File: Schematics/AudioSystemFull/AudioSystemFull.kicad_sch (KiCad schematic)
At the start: 285 parts, among them IC1 TDA1558Q, J1 SJ1-3515-SMT-TR-BE, J3 Conn_Display_Buttons, J6 Conn_ISO, U1 LP3856ES-5.0, U10 LT3015EQ-5PBF, U11 OPA2134, U12 OPA2134, U13 OPA2134, U14 OPA2134, U15 OPA2134, U16 OPA2134, U17 OPA2134, U18 OPA2134, U19 OPA2134, U2 DEVKIT_V1_ESP32-WROOM-32, U20 OPA2134, U21 OPA2134, U22 OPA2134, U23 OPA2134, U24 OPA2134, U25 OPA2134, U26 OPA2134, U27 OPA2134, U28 OPA2134, U3 PCM5102A, U4 OPA2134, U5 LP5907MFX-3.3, U6 LMR51420XFDDCR, U7 LMR51420YFDDCR, U8 LP5907MFX-3.3, U9 LMR51430YFDDCR

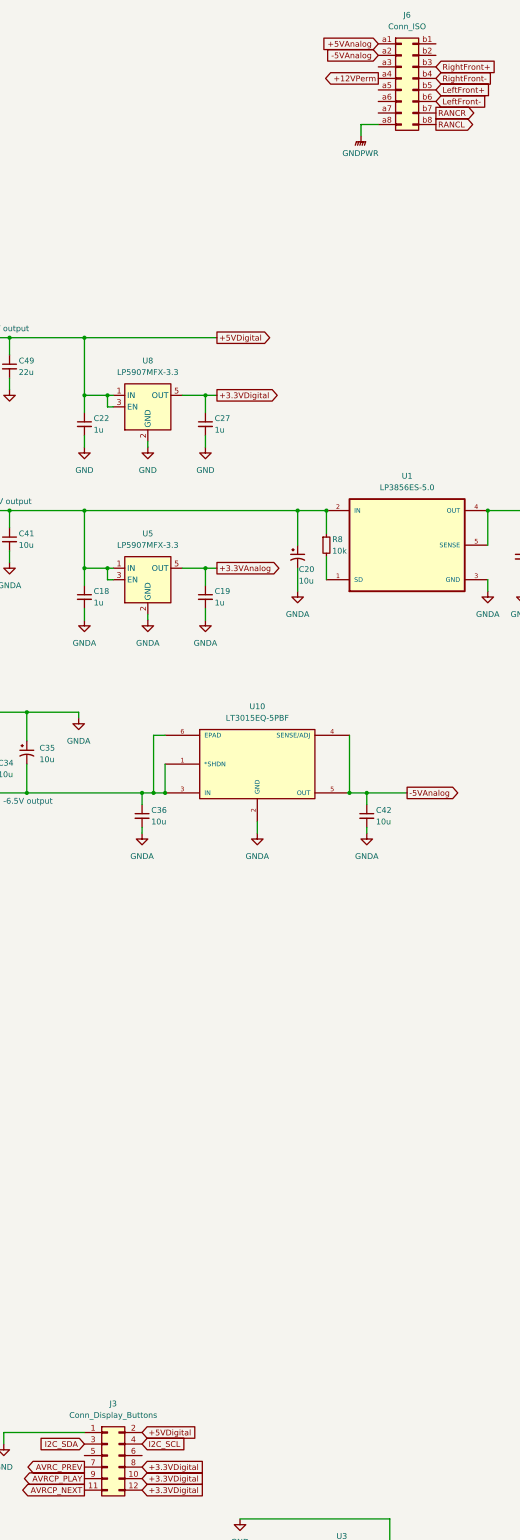
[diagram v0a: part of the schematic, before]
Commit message: organize footprints by purpose
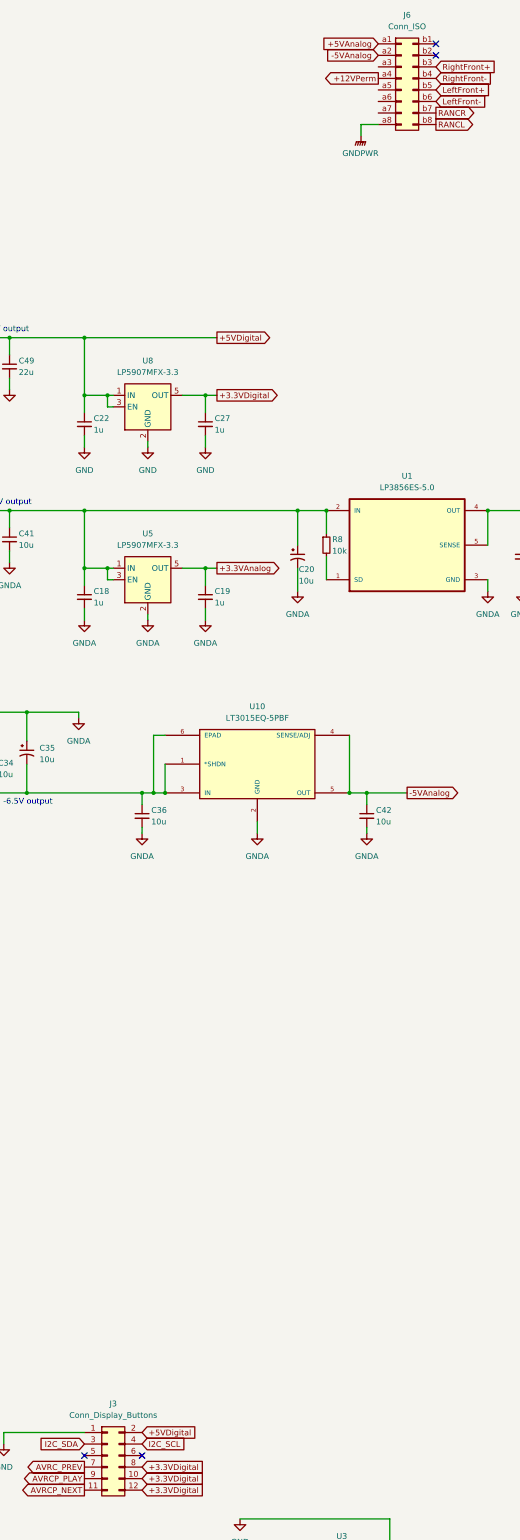
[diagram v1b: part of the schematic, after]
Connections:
- no-connect marks 30 -> 34
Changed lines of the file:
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@@
+	)
+	(no_connect
+		(at 273.05 35.56)
 	)
 	(no_connect
@@
 	)
 	(no_connect
+		(at 208.28 346.71)
+	)
+	(no_connect
 		(at 125.73 397.51)
 	)
@@
 	)
 	(no_connect
+		(at 273.05 38.1)
+	)
+	(no_connect
 		(at 166.37 369.57)
 	)
@@
 	)
 	(no_connect
+		(at 195.58 346.71)
+	)
+	(no_connect

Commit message: footprint placement part 1
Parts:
- C11, C12, C3, C4: footprint AudioSystemFootprintLibrary:UCZ1J100MCL1GS -> Capacitor_SMD:C_1206_3216Metric_Pad1.33x1.80mm_HandSolder; MANUFACTURER_PART_NUMBER UCZ1J100MCL1GS -> 293D106X96R3A2TE3
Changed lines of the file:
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@@
 			)
 		)
-		(property "Footprint" "AudioSystemFootprintLibrary:UCZ1J100MCL1GS"
+		(property "Footprint" "Capacitor_SMD:C_1206_3216Metric_Pad1.33x1.80mm_HandSolder"
 			(at 218.44 405.13 0)
 			(effects
@@
 			)
 		)
-		(property "MANUFACTURER_PART_NUMBER" "UCZ1J100MCL1GS"
+		(property "MANUFACTURER_PART_NUMBER" "293D106X96R3A2TE3"
 			(at 218.44 405.13 0)
 			(effects
@@
 			)
 		)
-		(property "Footprint" "AudioSystemFootprintLibrary:UCZ1J100MCL1GS"
+		(property "Footprint" "Capacitor_SMD:C_1206_3216Metric_Pad1.33x1.80mm_HandSolder"
 			(at 279.4 401.32 0)
 			(effects
@@
 			)
 		)
-		(property "MANUFACTURER_PART_NUMBER" "UCZ1J100MCL1GS"
+		(property "MANUFACTURER_PART_NUMBER" "293D106X96R3A2TE3"
 			(at 279.4 401.32 0)
 			(effects
@@
 			)
 		)
-		(property "Footprint" "AudioSystemFootprintLibrary:UCZ1J100MCL1GS"
+		(property "Footprint" "Capacitor_SMD:C_1206_3216Metric_Pad1.33x1.80mm_HandSolder"
 			(at 218.44 394.97 0)
 			(effects
@@
 			)
 		)
-		(property "MANUFACTURER_PART_NUMBER" "UCZ1J100MCL1GS"
+		(property "MANUFACTURER_PART_NUMBER" "293D106X96R3A2TE3"
 			(at 218.44 394.97 0)
 			(effects
@@
 			)
 		)
-		(property "Footprint" "AudioSystemFootprintLibrary:UCZ1J100MCL1GS"
+		(property "Footprint" "Capacitor_SMD:C_1206_3216Metric_Pad1.33x1.80mm_HandSolder"
 			(at 279.4 373.38 0)
 			(effects
@@
 			)
 		)
-		(property "MANUFACTURER_PART_NUMBER" "UCZ1J100MCL1GS"
+		(property "MANUFACTURER_PART_NUMBER" "293D106X96R3A2TE3"
 			(at 279.4 373.38 0)
 			(effects

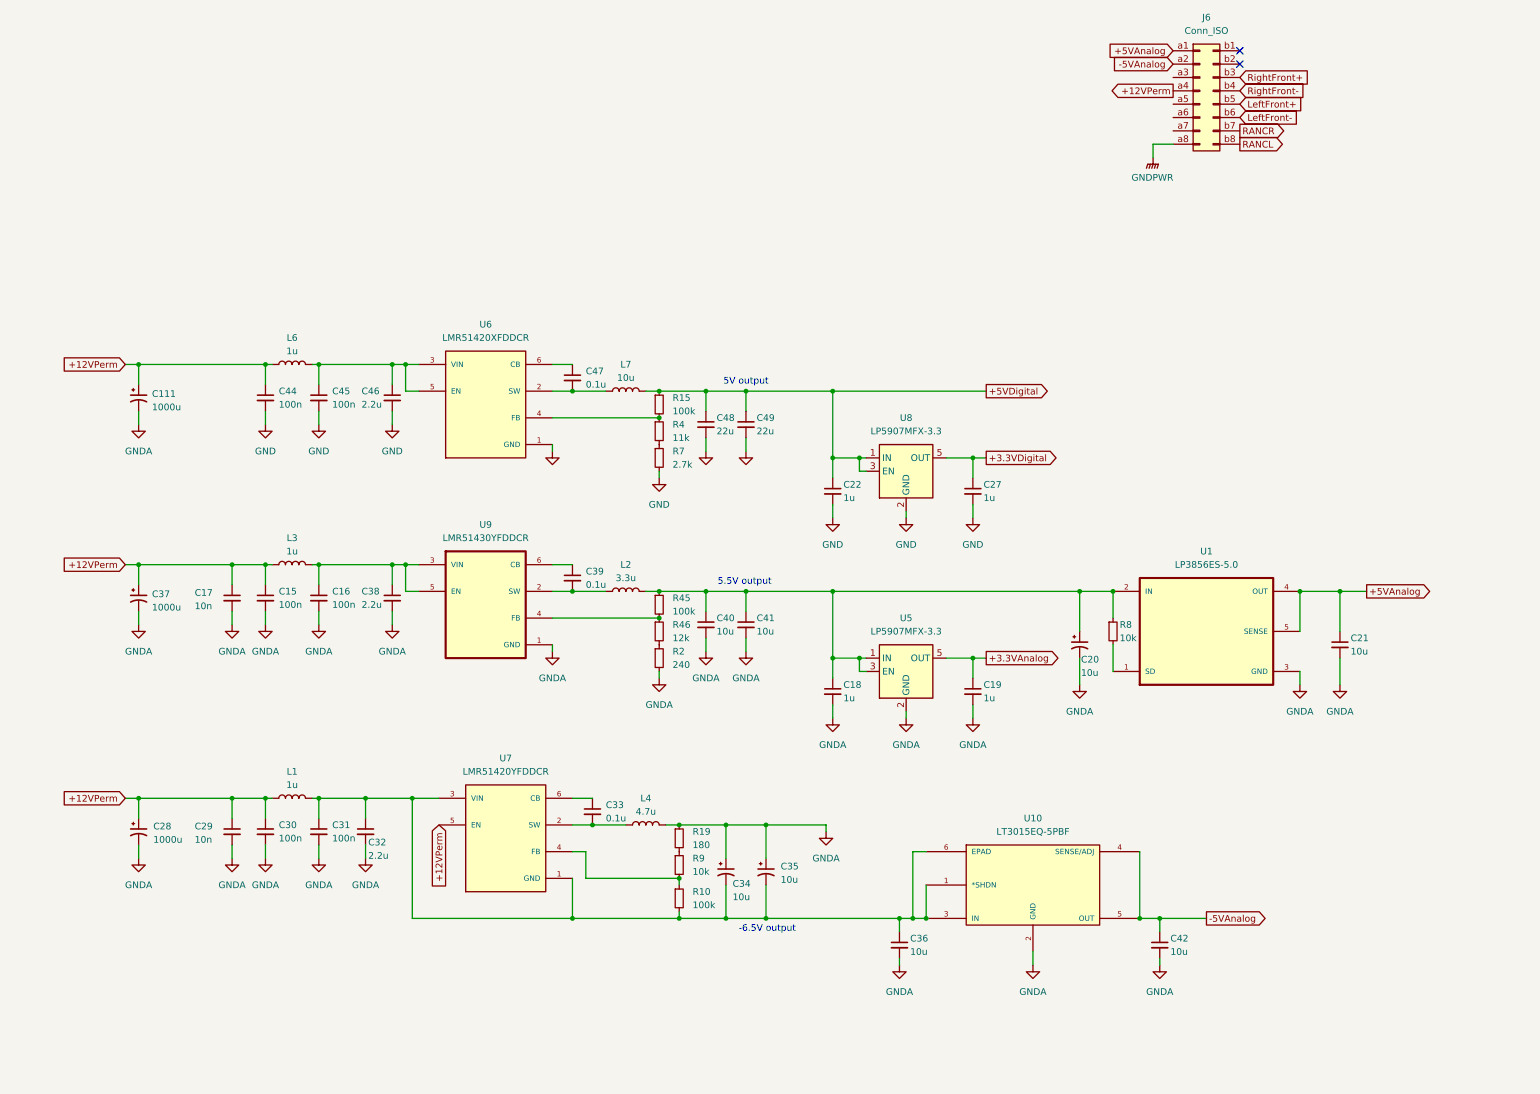
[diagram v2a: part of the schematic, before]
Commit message: footprint placement possibly done, minor schematic changes
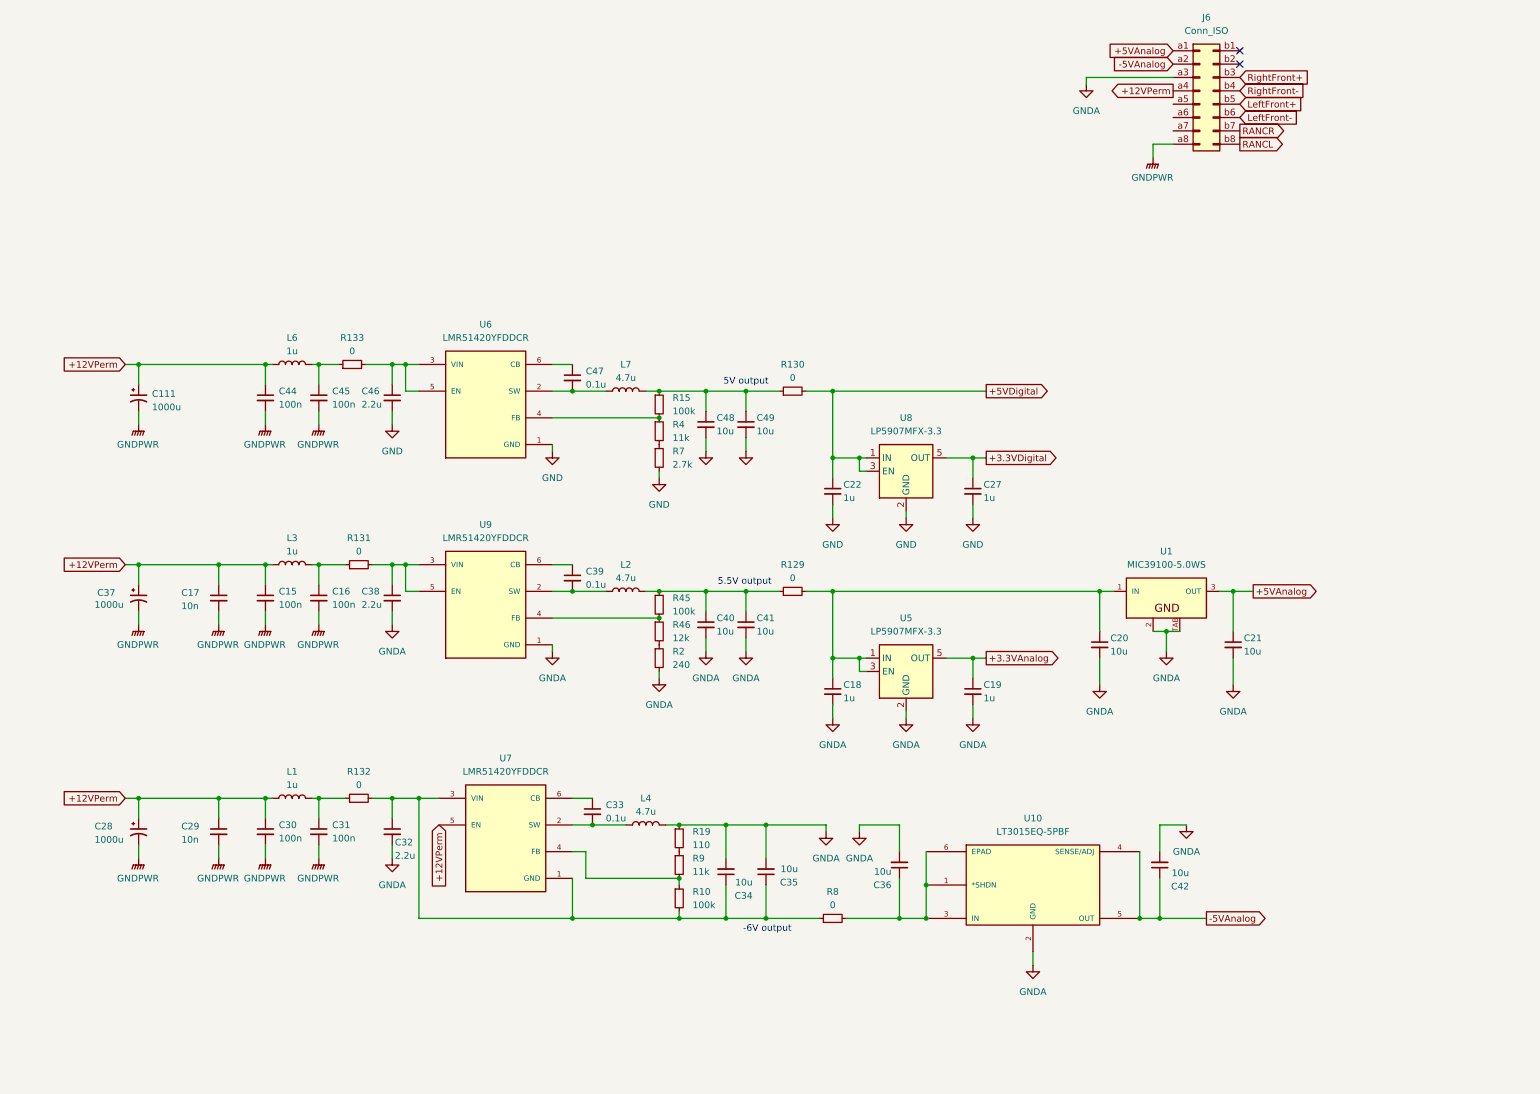
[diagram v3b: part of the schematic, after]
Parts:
- removed C20, C34, C35: 10u, AudioSystemFootprintLibrary:UCZ1J100MCL1GS, symbol Device:C_Polarized_Small_US
- removed U1: LP3856ES-5.0, AudioSystemFootprintLibrary:LP3856ES-5.0, symbol AudioSystemSymbolLibrary:LP3856ES-5.0
- removed U6: LMR51420XFDDCR, AudioSystemFootprintLibrary:LMR51420XFDDCR, symbol AudioSystemSymbolLibrary:LMR51420XFDDCR
- removed U9: LMR51430YFDDCR, AudioSystemFootprintLibrary:LMR51430YFDDCR, symbol AudioSystemSymbolLibrary:LMR51430YFDDCR
- added C20, C34, C35: 10u, Capacitor_SMD:C_0805_2012Metric_Pad1.18x1.45mm_HandSolder, symbol Device:C_Small
- added R129, R130, R131, R132, R133: 0, Resistor_SMD:R_0805_2012Metric_Pad1.20x1.40mm_HandSolder, symbol Device:R_Small
- added U1: MIC39100-5.0WS, AudioSystemFootprintLibrary:MIC39100-5.0WS, symbol AudioSystemSymbolLibrary:MIC39100-5.0WS
- added U6, U9: LMR51420YFDDCR, AudioSystemFootprintLibrary:LMR51420YFDDCR, symbol AudioSystemSymbolLibrary:LMR51420YFDDCR
- C1, C10, C100, C101, C102, C103, C104, C105, C106, C107, C108, C109, C110, C13, C14, C15, C16, C17, C18, C19, C2, C21, C22, C23, C24, C25, C27, C29, C30, C31, C32, C33, C36, C38, C39, C40, C41, C42, C43, C44, C45, C46, C47, C5, C50, C51, C52, C53, C54, C55, C56, C57, C58, C59, C6, C60, C61, C62, C63, C64, C65, C66, C67, C68, C69, C7, C70, C71, C72, C73, C74, C75, C76, C77, C78, C79, C8, C80, C81, C82, C83, C84, C85, C86, C87, C88, C89, C9, C90, C91, C92, C93, C94, C95, C96, C97, C98, C99: footprint Capacitor_SMD:C_1206_3216Metric_Pad1.33x1.80mm_HandSolder -> Capacitor_SMD:C_0805_2012Metric_Pad1.18x1.45mm_HandSolder
- C48, C49: value 22u -> 10u; footprint Capacitor_SMD:C_1210_3225Metric_Pad1.33x2.70mm_HandSolder -> Capacitor_SMD:C_0805_2012Metric_Pad1.18x1.45mm_HandSolder; MANUFACTURER_PART_NUMBER CL32B226KAJNNNE -> (none)
- L2: value 3.3u -> 4.7u; footprint AudioSystemFootprintLibrary:SRP5030T-3R3M -> AudioSystemFootprintLibrary:VLS6045EX-4R7M-H; MANUFACTURER_PART_NUMBER SRP5030T-3R3M -> (none)
- L7: value 10u -> 4.7u; footprint AudioSystemFootprintLibrary:SRR1280A-100M -> AudioSystemFootprintLibrary:VLS6045EX-4R7M-H; MANUFACTURER_PART_NUMBER SRR1280A-100M -> (none)
- R1, R10, R100, R101, R102, R103, R104, R105, R106, R107, R108, R109, R11, R110, R111, R112, R113, R114, R115, R116, R117, R118, R119, R12, R120, R121, R122, R123, R124, R125, R126, R127, R128, R13, R14, R15, R16, R17, R18, R2, R20, R21, R23, R25, R26, R27, R28, R29, R3, R30, R31, R33, R35, R36, R37, R38, R39, R4, R40, R41, R42, R43, R44, R45, R46, R47, R48, R49, R5, R50, R51, R53, R55, R56, R57, R58, R59, R6, R60, R61, R62, R63, R64, R65, R66, R67, R68, R69, R7, R70, R73, R74, R75, R76, R77, R78, R79, R80, R83, R84, R85, R86, R87, R88, R89, R90, R91, R92, R93, R94, R95, R96, R99: footprint Resistor_SMD:R_1206_3216Metric_Pad1.30x1.75mm_HandSolder -> Resistor_SMD:R_0805_2012Metric_Pad1.20x1.40mm_HandSolder
- R19: value 180 -> 110; footprint Resistor_SMD:R_1206_3216Metric_Pad1.30x1.75mm_HandSolder -> Resistor_SMD:R_0805_2012Metric_Pad1.20x1.40mm_HandSolder
- R8: value 10k -> 0; footprint Resistor_SMD:R_1206_3216Metric_Pad1.30x1.75mm_HandSolder -> Resistor_SMD:R_0805_2012Metric_Pad1.20x1.40mm_HandSolder; MANUFACTURER_PART_NUMBER RNCU1206BTE10K0 -> HRG3216P-1800-D-T1
- R9: value 10k -> 11k; footprint Resistor_SMD:R_1206_3216Metric_Pad1.30x1.75mm_HandSolder -> Resistor_SMD:R_0805_2012Metric_Pad1.20x1.40mm_HandSolder
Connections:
- net +5VAnalog: now also U1.3 (OUT)
- net +5VDigital: now also R130.2; no longer C48.1, C49.1, L7.2, R15.1
- net GND: now also U6.1 (GND); no longer C44.2, C45.2
- net GNDA: now also J6.a3 (Pin_a3), C20.2, C34.2, C35.2, U1.2, U1.TAB, U9.1 (GND); no longer C111.2, C15.2, C16.2, C17.2, C28.2, C29.2, C30.2, C31.2, C37.2
- net GNDPWR: now also C111.2, C15.2, C16.2, C17.2, C28.2, C29.2, C30.2, C31.2, C37.2, C44.2, C45.2
- net at C45.1, L6.2: now also R133.1; no longer C46.1
- net at C40.1, C41.1, L2.2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: now also R129.1; no longer C18.1, R8.1, U5.1 (IN), U5.3 (EN)
- net at C47.2, L7.1: now also U6.2 (SW)
- net at R15.2, R4.1: now also U6.4 (FB)
- net at C47.1: now also U6.6 (CB)
- net at C16.1, L3.2: now also R131.1; no longer C38.1
- net at C39.2, L2.1: now also U9.2 (SW)
- net at R8.2: now also C36.1, U10.1 (*SHDN), U10.3 (IN), U10.6 (EPAD)
- net at R45.2, R46.1: now also U9.4 (FB)
- net at C39.1: now also U9.6 (CB)
- new net: C32.1, C34.1, C35.1, R10.2, R132.2, R8.1, U7.1 (GND), U7.3 (VIN)
- new net: C18.1, C20.1, R129.2, U1.1 (IN), U5.1 (IN), U5.3 (EN)
- new net: C46.1, R133.2, U6.3 (VIN), U6.5 (EN)
- new net: C48.1, C49.1, L7.2, R130.1, R15.1
- new net: C38.1, R131.2, U9.3 (VIN), U9.5 (EN)
- new net: C31.1, L1.2, R132.1
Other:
- note added: "-6V output"
- note removed: "-6.5V output"
- moved on the sheet: C17, C21, C29, C32, C36, C42

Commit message: progress sync
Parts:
- removed C11, C12, C3, C4: 10u, Capacitor_SMD:C_1206_3216Metric_Pad1.33x1.80mm_HandSolder, symbol Device:C_Polarized_Small_US
- added C11, C12, C3, C4: 10u, Capacitor_SMD:C_0805_2012Metric_Pad1.18x1.45mm_HandSolder, symbol Device:C_Small
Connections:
- net +3.3VAnalog: now also C11.2, C12.2
- net +3.3VDigital: now also C4.2
- net AVRCP_NEXT: now also J3.7 (Pin_7), U2.30 (IO18); no longer J3.11 (Pin_11), U2.31 (IO19)
- net AVRCP_PLAY: now also U2.31 (IO19); no longer U2.30 (IO18)
- net AVRC_PREV: now also J3.11 (Pin_11); no longer J3.7 (Pin_7)
- net GND: now also C3.2, C4.1; no longer C25.1, C26.2
- net GNDA: now also C11.1, C12.1
- net GNDPWR: now also C25.1, C26.2
- net I2C_SCL: now also J3.6 (Pin_6); no longer J3.4 (Pin_4)
- net I2C_SDA: now also J3.5 (Pin_5); no longer J3.3 (Pin_3)
- net at C5.1, U3.18 (LDOO): now also C3.1

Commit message: pcbs done
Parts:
- added R134, R135: 10k, Resistor_SMD:R_0805_2012Metric_Pad1.20x1.40mm_HandSolder, symbol Device:R
- R1, R3: value 10k -> 100k; MANUFACTURER_PART_NUMBER RT1206DRE0710KL -> (none)
- R7: value 2.7k -> 2k; MANUFACTURER_PART_NUMBER HRG3216P-2701-D-T1 -> (none)
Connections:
- net +5VAnalog: now also J6.a2 (Pin_a2); no longer J6.a1 (Pin_a1)
- net -5VAnalog: now also J6.a1 (Pin_a1); no longer J6.a2 (Pin_a2)
- net GNDA: now also R134.1, R135.2
- net at C2.1, J1.3: now also R134.2
- net at C1.1, J1.2: now also R135.1
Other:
- note added: "5.2V output"
- note removed: "5V output"
- note removed: "R/FALowL - Raw/Filtered Audio Low frequency Left channel R/FAMidL - Raw/Filtered Audio Mid frequency Left channel R/FAHighL - Raw/Filtered Audio High frequency Left channel R/FALowR - Raw/Filtered Audio Low frequency Right channel R/FAMidR - Raw/Filtered Audio Mid frequency Right channel R/FAHighR - Raw/Filtered Audio High frequency Right channel FAL - Filtered Audio Left channel FAR - Filtered A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"
- moved on the sheet: C109, C110, C75, C76, R11, R111, R112, R12, R13, R14, R17, R18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
